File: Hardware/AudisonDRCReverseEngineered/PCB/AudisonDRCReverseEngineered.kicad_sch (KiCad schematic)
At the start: 55 parts, among them J1 Conn_01x06, J2 PROG PADS REAR, Q1 AO3400A, Q2 AO3400A, SW1 SW_MEC_5G_LED, SW2 SW_MEC_5G_LED, SW3 SW_MEC_5G_LED, SW4 SW_MEC_5G_LED, SW5 SW_MEC_5G_LED, U1 LP2950-5.0_TO252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

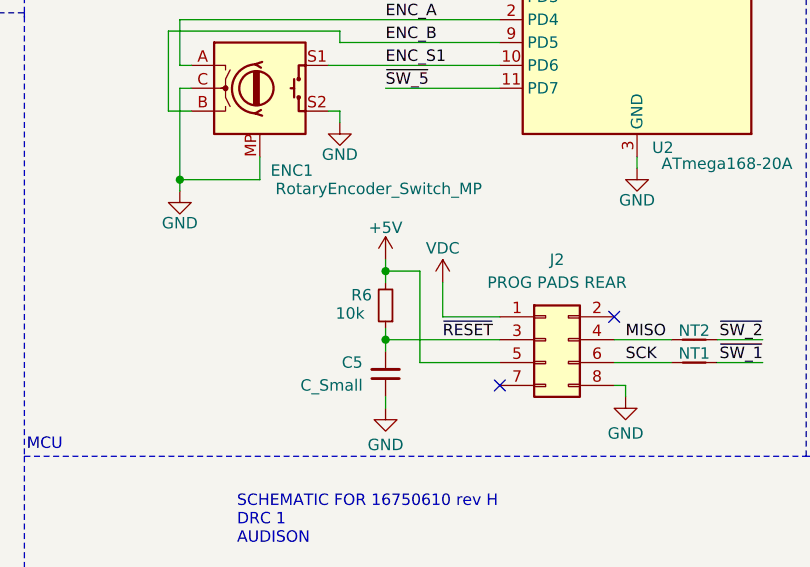
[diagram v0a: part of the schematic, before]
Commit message: Fix - updated the programming header. Header uses +5V not VDC as power input
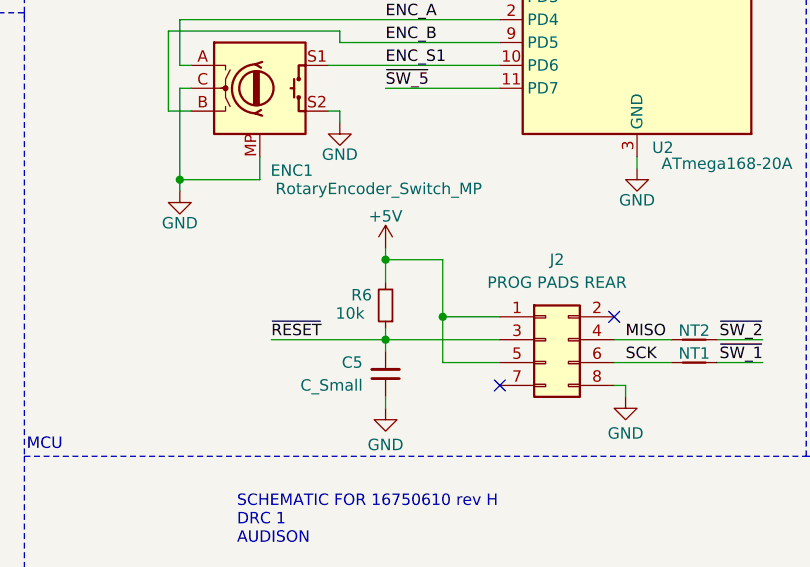
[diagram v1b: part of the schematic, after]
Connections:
- net +5V: now also J2.1 (Pin_1)
- net VDC: no longer J2.1 (Pin_1)
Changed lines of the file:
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@@
 	)
 	(junction
-		(at 194.31 143.51)
-		(diameter 0)
-		(color 0 0 0 0)
-	)
-	(junction
 		(at 95.25 57.15)
 		(diameter 0)
@@
 	)
 	(junction
+		(at 194.31 142.24)
+		(diameter 0)
+		(color 0 0 0 0)
+	)
+	(junction
 		(at 142.24 82.55)
 		(diameter 0)
@@
 	)
 	(junction
+		(at 200.66 148.59)
+		(diameter 0)
+		(color 0 0 0 0)
+	)
+	(junction
 		(at 76.2 148.59)
 		(diameter 0)
@@
 	(wire
 		(pts
-			(xy 194.31 143.51) (xy 194.31 144.78)
-		)
-		(stroke
-			(width 0)
-			(type default)
-		)
-	)
-	(wire
-		(pts
 			(xy 254 93.98) (xy 254 81.28)
 		)
@@
 	(wire
 		(pts
-			(xy 198.12 143.51) (xy 194.31 143.51)
-		)
-		(stroke
-			(width 0)
-			(type default)
-		)
-	)
-	(wire
-		(pts
 			(xy 99.06 55.88) (xy 99.06 57.15)
 		)
@@
 	(wire
 		(pts
-			(xy 198.12 153.67) (xy 207.01 153.67)
+			(xy 200.66 153.67) (xy 207.01 153.67)
 		)
 		(stroke
@@
 	(wire
 		(pts
+			(xy 181.61 151.13) (xy 194.31 151.13)
+		)
+		(stroke
+			(width 0)
+			(type default)
+		)
+	)
+	(wire
+		(pts
 			(xy 71.12 25.4) (xy 78.74 25.4)
 		)
@@
 	(wire
 		(pts
+			(xy 194.31 142.24) (xy 194.31 144.78)
+		)
+		(stroke
+			(width 0)
+			(type default)
+		)
+	)
+	(wire
+		(pts
 			(xy 114.3 161.29) (xy 114.3 170.18)
 		)
@@
 	(wire
 		(pts
-			(xy 198.12 143.51) (xy 198.12 153.67)
+			(xy 200.66 142.24) (xy 200.66 148.59)
 		)
 		(stroke
@@
 	(wire
 		(pts
+			(xy 200.66 148.59) (xy 200.66 153.67)
+		)
+		(stroke
+			(width 0)
+			(type default)
+		)
+	)
+	(wire
+		(pts
 			(xy 76.2 148.59) (xy 76.2 135.89)
 		)
@@
 	(wire
 		(pts
-			(xy 194.31 142.24) (xy 194.31 143.51)
+			(xy 194.31 140.97) (xy 194.31 142.24)
 		)
 		(stroke
@@
 	(wire
 		(pts
-			(xy 200.66 144.78) (xy 200.66 148.59)
-		)
-		(stroke
-			(width 0)
-			(type default)
-		)
-	)
-	(wire
-		(pts
 			(xy 106.68 35.56) (xy 96.52 35.56)
 		)
@@
 	(wire
 		(pts
+			(xy 194.31 142.24) (xy 200.66 142.24)
+		)
+		(stroke
+			(width 0)
+			(type default)
+		)
+	)
+	(wire
+		(pts
 			(xy 194.31 151.13) (xy 207.01 151.13)
 		)
@@
 	)
 	(label "~{RESET}"
-		(at 200.66 151.13 0)
+		(at 181.61 151.13 0)
 		(fields_autoplaced yes)
 		(effects
@@
 	)
 	(symbol
-		(lib_id "power:VDC")
-		(at 200.66 144.78 0)
-		(unit 1)
-		(exclude_from_sim no)
-		(in_bom yes)
-		(on_board yes)
-		(dnp no)
-		(property "Reference" "#PWR024"
-			(at 200.66 148.59 0)
-			(effects
-				(font
-					(size 1.27 1.27)
-				)
-				(hide yes)
-			)
-		)
-		(property "Value" "VDC"
-			(at 200.66 140.97 0)
-			(effects
-				(font
-					(size 1.27 1.27)
-				)
-			)
-		)
-		(property "Footprint" ""
-			(at 200.66 144.78 0)
-			(effects
-				(font
-					(size 1.27 1.27)
-				)
-				(hide yes)
-			)
-		)
-		(property "Datasheet" ""
-			(at 200.66 144.78 0)
-			(effects
-				(font
-					(size 1.27 1.27)
-				)
-				(hide yes)
-			)
-		)
-		(property "Description" "Power symbol creates a global label with name \"VDC\""
-			(at 200.66 144.78 0)
-			(effects
-				(font
-					(size 1.27 1.27)
-				)
-				(hide yes)
-			)
-		)
-		(pin "1"
-		)
-		(instances
-			(project "AudisonDRCReverseEngineered"
-				(path "/2bdc53b7-c29d-4ef8-8e2c-89e6e1d74e69"
-					(reference "#PWR024")
-					(unit 1)
-				)
-			)
-		)
-	)
-	(symbol
 		(lib_id "Device:C_Small")
 		(at 44.45 69.85 0)
@@
 	(symbol
 		(lib_id "power:+5V")
-		(at 194.31 142.24 0)
+		(at 194.31 140.97 0)
 		(mirror y)
 		(unit 1)
@@
 		(dnp no)
 		(property "Reference" "#PWR026"
-			(at 194.31 146.05 0)
+			(at 194.31 144.78 0)
 			(effects
 				(font
@@
 		)
 		(property "Value" "+5V"
-			(at 194.31 138.684 0)
+			(at 194.31 137.414 0)
 			(effects
 				(font
@@
 		)
 		(property "Footprint" ""
-			(at 194.31 142.24 0)
+			(at 194.31 140.97 0)
 			(effects
 				(font
@@
 		)
 		(property "Datasheet" ""
-			(at 194.31 142.24 0)
+			(at 194.31 140.97 0)
 			(effects
 				(font
@@
 		)
 		(property "Description" "Power symbol creates a global label with name \"+5V\""
-			(at 194.31 142.24 0)
+			(at 194.31 140.97 0)
 			(effects
 				(font

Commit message: Update HW folder with latest work on rev B
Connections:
- net DSP_EN: now also R17.1; no longer R17.2
- net at D3.2 (A): now also R17.2; no longer R17.1
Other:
- moved on the sheet: D3, LED1, LED2, LED3, LED4, Q1, R1, R14, R15, R16, R17, SW1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
